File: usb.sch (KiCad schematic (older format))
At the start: 13 parts

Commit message: gpio assignment done
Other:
- note added: "tantalum cap"
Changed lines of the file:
@@
 $Descr A4 11693 8268
 encoding utf-8
-Sheet 8 10
+Sheet 7 10
 Title ""
 Date ""
@@
 Text Label 7500 3250 0    60   ~ 0
 USB1_PWR
+Text Notes 6625 4475 0    60   ~ 0
+tantalum cap
 $EndSCHEMATC

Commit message: annotation, wip erc
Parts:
- gave numbers to parts that had none: 13
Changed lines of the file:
@@
 $EndDescr
 $Comp
-L AM335X_ZCZ IC?
+L AM335X_ZCZ IC2
 U 11 1 58AF2AA9
 P 2300 2650
-F 0 "IC?" V 2250 2950 60  0000 C CNN
+F 0 "IC2" V 2250 2950 60  0000 C CNN
 F 1 "AM335X_ZCZ" V 2250 2350 60  0000 C CNN
 F 2 "footprints:PBGA_N324" H 2300 2650 60  0001 C CNN
@@
 	3800 2150 6025 2150
 $Comp
-L TPD4S012 U?
+L TPD4S012 U6
 U 1 1 58ACA818
 P 4400 3950
-F 0 "U?" H 4475 3700 60  0000 C CNN
+F 0 "U6" H 4475 3700 60  0000 C CNN
 F 1 "TPD4S012" H 4650 3600 60  0000 C CNN
 F 2 "" H 4425 4025 60  0001 C CNN
@@
 	3800 2350 6025 2350
 $Comp
-L USB_DC #PWR?
+L USB_DC #PWR253
 U 1 1 58ACAA5E
 P 4900 3450
-F 0 "#PWR?" H 4900 3300 50  0001 C CNN
+F 0 "#PWR253" H 4900 3300 50  0001 C CNN
 F 1 "USB_DC" H 4900 3600 50  0000 C CNN
 F 2 "" H 4900 3450 50  0000 C CNN
@@
 $EndComp
 $Comp
-L C C?
+L C C125
 U 1 1 58ACAA92
 P 4900 3850
-F 0 "C?" H 4925 3950 50  0000 L CNN
+F 0 "C125" H 4925 3950 50  0000 L CNN
 F 1 "100nF/6.3V" H 4925 3750 50  0000 L CNN
 F 2 "" H 4938 3700 50  0000 C CNN
@@
 Connection ~ 4900 3500
 $Comp
-L GNDD #PWR?
+L GNDD #PWR250
 U 1 1 58ACAB63
 P 4400 4425
-F 0 "#PWR?" H 4400 4175 50  0001 C CNN
+F 0 "#PWR250" H 4400 4175 50  0001 C CNN
 F 1 "GNDD" H 4400 4275 50  0000 C CNN
 F 2 "" H 4400 4425 50  0000 C CNN
@@
 NoConn ~ 3800 2450
 $Comp
-L R R?
+L R R52
 U 1 1 58ACACC5
 P 4675 2250
-F 0 "R?" V 4625 2050 50  0000 C CNN
+F 0 "R52" V 4625 2050 50  0000 C CNN
 F 1 "0R" V 4675 2250 50  0000 C CNN
 F 2 "" V 4605 2250 50  0000 C CNN
@@
 $EndComp
 $Comp
-L USB_DC #PWR?
+L USB_DC #PWR251
 U 1 1 58ACAD7C
 P 4825 2250
-F 0 "#PWR?" H 4825 2100 50  0001 C CNN
+F 0 "#PWR251" H 4825 2100 50  0001 C CNN
 F 1 "USB_DC" V 4825 2500 50  0000 C CNN
 F 2 "" H 4825 2250 50  0000 C CNN
@@
 	4525 2250 3800 2250
 $Comp
-L TPD4S012 U?
+L TPD4S012 U7
 U 1 1 58ACB0F7
 P 5700 3950
-F 0 "U?" H 5775 3700 60  0000 C CNN
+F 0 "U7" H 5775 3700 60  0000 C CNN
 F 1 "TPD4S012" H 5950 3600 60  0000 C CNN
 F 2 "" H 5725 4025 60  0001 C CNN
@@
 $EndComp
 $Comp
-L C C?
+L C C126
 U 1 1 58ACB106
 P 6200 3850
-F 0 "C?" H 6225 3950 50  0000 L CNN
+F 0 "C126" H 6225 3950 50  0000 L CNN
 F 1 "100nF/6.3V" H 6225 3750 50  0000 L CNN
 F 2 "" H 6238 3700 50  0000 C CNN
@@
 	6200 3250 6200 3700
 $Comp
-L GNDD #PWR?
+L GNDD #PWR254
 U 1 1 58ACB114
 P 5700 4425
-F 0 "#PWR?" H 5700 4175 50  0001 C CNN
+F 0 "#PWR254" H 5700 4175 50  0001 C CNN
 F 1 "GNDD" H 5700 4275 50  0000 C CNN
 F 2 "" H 5700 4425 50  0000 C CNN
@@
 NoConn ~ 3800 3250
 $Comp
-L R R?
+L R R53
 U 1 1 58ACB512
 P 4675 3050
-F 0 "R?" V 4775 3050 50  0000 C CNN
+F 0 "R53" V 4775 3050 50  0000 C CNN
 F 1 "0R" V 4675 3050 50  0000 C CNN
 F 2 "" V 4605 3050 50  0000 C CNN
@@
 	4525 3050 3800 3050
 $Comp
-L GNDD #PWR?
+L GNDD #PWR252
 U 1 1 58ACB72B
 P 4825 3050
-F 0 "#PWR?" H 4825 2800 50  0001 C CNN
+F 0 "#PWR252" H 4825 2800 50  0001 C CNN
 F 1 "GNDD" V 4825 2850 50  0000 C CNN
 F 2 "" H 4825 3050 50  0000 C CNN
@@
 Connection ~ 5650 2850
 $Comp
-L TPS2065CDGN U?
+L TPS2065CDGN U8
 U 1 1 58ACBDB9
 P 7800 3925
-F 0 "U?" H 7625 4300 60  0000 C CNN
+F 0 "U8" H 7625 4300 60  0000 C CNN
 F 1 "TPS2065CDGN" H 7875 4200 60  0000 C CNN
 F 2 "" H 7550 3600 60  0001 C CNN
@@
 	3800 2950 6950 2950
 $Comp
-L L L?
+L L L9
 U 1 1 58ACBFF2
 P 7100 2950
-F 0 "L?" V 7050 2950 50  0000 C CNN
+F 0 "L9" V 7050 2950 50  0000 C CNN
 F 1 "0.1ohm 0805" V 7175 2950 50  0000 C CNN
 F 2 "" H 7100 2950 50  0000 C CNN
@@
 $EndComp
 $Comp
-L L L?
+L L L10
 U 1 1 58ACC1B4
 P 8875 2950
-F 0 "L?" V 8825 2950 50  0000 C CNN
+F 0 "L10" V 8825 2950 50  0000 C CNN
 F 1 "150ohm 1000mA" V 8950 2950 50  0000 C CNN
 F 2 "" H 8875 2950 50  0000 C CNN
@@
 	7350 3975 7350 4825
 $Comp
-L R R?
+L R R54
 U 1 1 58ACC71E
 P 7350 4975
-F 0 "R?" V 7430 4975 50  0000 C CNN
+F 0 "R54" V 7430 4975 50  0000 C CNN
 F 1 "10k" V 7350 4975 50  0000 C CNN
 F 2 "" V 7280 4975 50  0000 C CNN
@@
 Connection ~ 7350 4775
 $Comp
-L GNDD #PWR?
+L GNDD #PWR257
 U 1 1 58ACC7E4
 P 7350 5125
-F 0 "#PWR?" H 7350 4875 50  0001 C CNN
+F 0 "#PWR257" H 7350 4875 50  0001 C CNN
 F 1 "GNDD" H 7350 4975 50  0000 C CNN
 F 2 "" H 7350 5125 50  0000 C CNN
@@
 $EndComp
 $Comp
-L CP C?
+L CP C127
 U 1 1 58ACC8FE
 P 6850 4025
-F 0 "C?" H 6875 4125 50  0000 L CNN
+F 0 "C127" H 6875 4125 50  0000 L CNN
 F 1 "220uF/6.3V" H 6875 3925 50  0000 L CNN
 F 2 "Capacitors_Tantalum_SMD:CP_Tantalum_Case-A_EIA-3216-18_Reflow" H 6888 3875 50  0001 C CNN
@@
 Connection ~ 7300 3775
 $Comp
-L GNDD #PWR?
+L GNDD #PWR256
 U 1 1 58ACCD7F
 P 6850 4175
-F 0 "#PWR?" H 6850 3925 50  0001 C CNN
+F 0 "#PWR256" H 6850 3925 50  0001 C CNN
 F 1 "GNDD" H 6850 4025 50  0000 C CNN
 F 2 "" H 6850 4175 50  0000 C CNN
@@
 $EndComp
 $Comp
-L SYS_5V #PWR?
+L SYS_5V #PWR255
 U 1 1 58ACCF48
 P 6850 3725
-F 0 "#PWR?" H 6850 3575 50  0001 C CNN
+F 0 "#PWR255" H 6850 3575 50  0001 C CNN
 F 1 "SYS_5V" H 6850 3875 50  0000 C CNN
 F 2 "" H 6850 3725 50  0000 C CNN
@@
 Connection ~ 8350 3775
 $Comp
-L GNDD #PWR?
+L GNDD #PWR258
 U 1 1 58ACD3E3
 P 7800 4575
-F 0 "#PWR?" H 7800 4325 50  0001 C CNN
+F 0 "#PWR258" H 7800 4325 50  0001 C CNN
 F 1 "GNDD" H 7800 4425 50  0000 C CNN
 F 2 "" H 7800 4575 50  0000 C CNN
@@
 Connection ~ 7800 4525
 $Comp
-L R R?
+L R R55
 U 1 1 58ACD6CF
 P 8600 3875
-F 0 "R?" V 8680 3875 50  0000 C CNN
+F 0 "R55" V 8680 3875 50  0000 C CNN
 F 1 "10k" V 8600 3875 50  0000 C CNN
 F 2 "" V 8530 3875 50  0000 C CNN
@@
 $EndComp
 $Comp
-L VDD_3V3A #PWR?
+L VDD_3V3A #PWR259
 U 1 1 58ACD7EC
 P 8600 3725
-F 0 "#PWR?" H 8600 3575 50  0001 C CNN
+F 0 "#PWR259" H 8600 3575 50  0001 C CNN
 F 1 "VDD_3V3A" H 8600 3875 50  0000 C CNN
 F 2 "" H 8600 3725 50  0000 C CNN

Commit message: erc passed, sch first version
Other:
- moved on the sheet: L10
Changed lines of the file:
@@
 	3800 2350 6025 2350
 $Comp
-L USB_DC #PWR253
+L USB_DC #PWR0269
 U 1 1 58ACAA5E
 P 4900 3450
-F 0 "#PWR253" H 4900 3300 50  0001 C CNN
+F 0 "#PWR0269" H 4900 3300 50  0001 C CNN
 F 1 "USB_DC" H 4900 3600 50  0000 C CNN
 F 2 "" H 4900 3450 50  0000 C CNN
@@
 Connection ~ 4900 3500
 $Comp
-L GNDD #PWR250
+L GNDD #PWR0270
 U 1 1 58ACAB63
 P 4400 4425
-F 0 "#PWR250" H 4400 4175 50  0001 C CNN
+F 0 "#PWR0270" H 4400 4175 50  0001 C CNN
 F 1 "GNDD" H 4400 4275 50  0000 C CNN
 F 2 "" H 4400 4425 50  0000 C CNN
@@
 $EndComp
 $Comp
-L USB_DC #PWR251
+L USB_DC #PWR0271
 U 1 1 58ACAD7C
 P 4825 2250
-F 0 "#PWR251" H 4825 2100 50  0001 C CNN
+F 0 "#PWR0271" H 4825 2100 50  0001 C CNN
 F 1 "USB_DC" V 4825 2500 50  0000 C CNN
 F 2 "" H 4825 2250 50  0000 C CNN
@@
 	6200 3250 6200 3700
 $Comp
-L GNDD #PWR254
+L GNDD #PWR0272
 U 1 1 58ACB114
 P 5700 4425
-F 0 "#PWR254" H 5700 4175 50  0001 C CNN
+F 0 "#PWR0272" H 5700 4175 50  0001 C CNN
 F 1 "GNDD" H 5700 4275 50  0000 C CNN
 F 2 "" H 5700 4425 50  0000 C CNN
@@
 	4525 3050 3800 3050
 $Comp
-L GNDD #PWR252
+L GNDD #PWR0273
 U 1 1 58ACB72B
 P 4825 3050
-F 0 "#PWR252" H 4825 2800 50  0001 C CNN
+F 0 "#PWR0273" H 4825 2800 50  0001 C CNN
 F 1 "GNDD" V 4825 2850 50  0000 C CNN
 F 2 "" H 4825 3050 50  0000 C CNN
@@
 L L L10
 U 1 1 58ACC1B4
-P 8875 2950
-F 0 "L10" V 8825 2950 50  0000 C CNN
-F 1 "150ohm 1000mA" V 8950 2950 50  0000 C CNN
-F 2 "" H 8875 2950 50  0000 C CNN
-F 3 "" H 8875 2950 50  0000 C CNN
-	1    8875 2950
+P 8800 2950
+F 0 "L10" V 8750 2950 50  0000 C CNN
+F 1 "150ohm 1000mA" V 8875 2950 50  0000 C CNN
+F 2 "" H 8800 2950 50  0000 C CNN
+F 3 "" H 8800 2950 50  0000 C CNN
+	1    8800 2950
 	0    1    1    0
 $EndComp
@@
 USB1_VBUS
 Wire Wire Line
-	9300 2950 9025 2950
-Wire Wire Line
-	7250 2950 8725 2950
+	8950 2950 9300 2950
+Wire Wire Line
+	7250 2950 8650 2950
 Wire Wire Line
 	3800 3150 3925 3150
@@
 Connection ~ 7350 4775
 $Comp
-L GNDD #PWR257
+L GNDD #PWR0274
 U 1 1 58ACC7E4
 P 7350 5125
-F 0 "#PWR257" H 7350 4875 50  0001 C CNN
+F 0 "#PWR0274" H 7350 4875 50  0001 C CNN
 F 1 "GNDD" H 7350 4975 50  0000 C CNN
 F 2 "" H 7350 5125 50  0000 C CNN
@@
 Connection ~ 7300 3775
 $Comp
-L GNDD #PWR256
+L GNDD #PWR0275
 U 1 1 58ACCD7F
 P 6850 4175
-F 0 "#PWR256" H 6850 3925 50  0001 C CNN
+F 0 "#PWR0275" H 6850 3925 50  0001 C CNN
 F 1 "GNDD" H 6850 4025 50  0000 C CNN
 F 2 "" H 6850 4175 50  0000 C CNN
@@
 $EndComp
 $Comp
-L SYS_5V #PWR255
+L SYS_5V #PWR0276
 U 1 1 58ACCF48
 P 6850 3725
-F 0 "#PWR255" H 6850 3575 50  0001 C CNN
+F 0 "#PWR0276" H 6850 3575 50  0001 C CNN
 F 1 "SYS_5V" H 6850 3875 50  0000 C CNN
 F 2 "" H 6850 3725 50  0000 C CNN
@@
 Connection ~ 8350 3775
 $Comp
-L GNDD #PWR258
+L GNDD #PWR0277
 U 1 1 58ACD3E3
 P 7800 4575
-F 0 "#PWR258" H 7800 4325 50  0001 C CNN
+F 0 "#PWR0277" H 7800 4325 50  0001 C CNN
 F 1 "GNDD" H 7800 4425 50  0000 C CNN
 F 2 "" H 7800 4575 50  0000 C CNN
@@
 $EndComp
 $Comp
-L VDD_3V3A #PWR259
+L VDD_3V3A #PWR0278
 U 1 1 58ACD7EC
 P 8600 3725
-F 0 "#PWR259" H 8600 3575 50  0001 C CNN
+F 0 "#PWR0278" H 8600 3575 50  0001 C CNN
 F 1 "VDD_3V3A" H 8600 3875 50  0000 C CNN
 F 2 "" H 8600 3725 50  0000 C CNN
@@
 Text Notes 6625 4475 0    60   ~ 0
 tantalum cap
+$Comp
+L PWR_FLAG #FLG0279
+U 1 1 58C56F63
+P 9250 3025
+F 0 "#FLG0279" H 9250 3100 50  0001 C CNN
+F 1 "PWR_FLAG" H 9250 3175 50  0000 C CNN
+F 2 "" H 9250 3025 50  0001 C CNN
+F 3 "" H 9250 3025 50  0001 C CNN
+	1    9250 3025
+	-1   0    0    1
+$EndComp
+Wire Wire Line
+	9250 3025 9250 2950
+Connection ~ 9250 2950
 $EndSCHEMATC

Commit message: wip sys and power
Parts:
- removed IC2: AM335X_ZCZ, footprints:PBGA_N324, symbol AM335X_ZCZ
- added C?: 100nF/6.3V, symbol C
- added IC?: OSD335x, GHI-SoMs-Processors_OSD3358, symbol OSD335x
- added IC?: SN74LVC2G241DCUR, symbol LOGIC-2G125_Dual_3ST_NonInv_Buffer
- added R?: 100k, symbol R
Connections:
- net GNDD: now also C?.2, IC?.1 (n1OE), IC?.4 (GND), R?.2
- net USB0_DM: now also IC?.N18 (USB0_DM)
- net USB0_DP: now also IC?.N17 (USB0_DP)
- net USB0_ID: now also IC?.P16 (USB0_ID)
- net USB1_DM: now also IC?.R18 (USB1_DM)
- net USB1_DP: now also IC?.R17 (USB1_DP)
- net USB1_DRVVBUS: now also IC?.F15 (USB1_DRVVBUS)
- net at R52.2: now also IC?.P15 (USB0_VBUS)
- net at R53.2: now also IC?.P17 (USB1_ID)
- net at L9.2: now also IC?.T18 (USB1_VBUS)
- new net UART0_RXD: IC?.2 (1A), R?.1
- new net UART0_RXD.CPU: IC?.6 (1Y), IC?.E15 (UART0_RXD)
- new net UART0_TXD: IC?.3 (2Y)
- new net UART0_TXD.CPU: IC?.5 (2A), IC?.E16 (UART0_TXD)
- new net VDD_3V3B: C?.1, IC?.7 (2OE), IC?.8 (VCC)
- no-connect marks 4 -> 6
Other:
- moved on the sheet: C125, C126, C127, L10, L9, R52, R53, R54, R55, U6, U7, U8

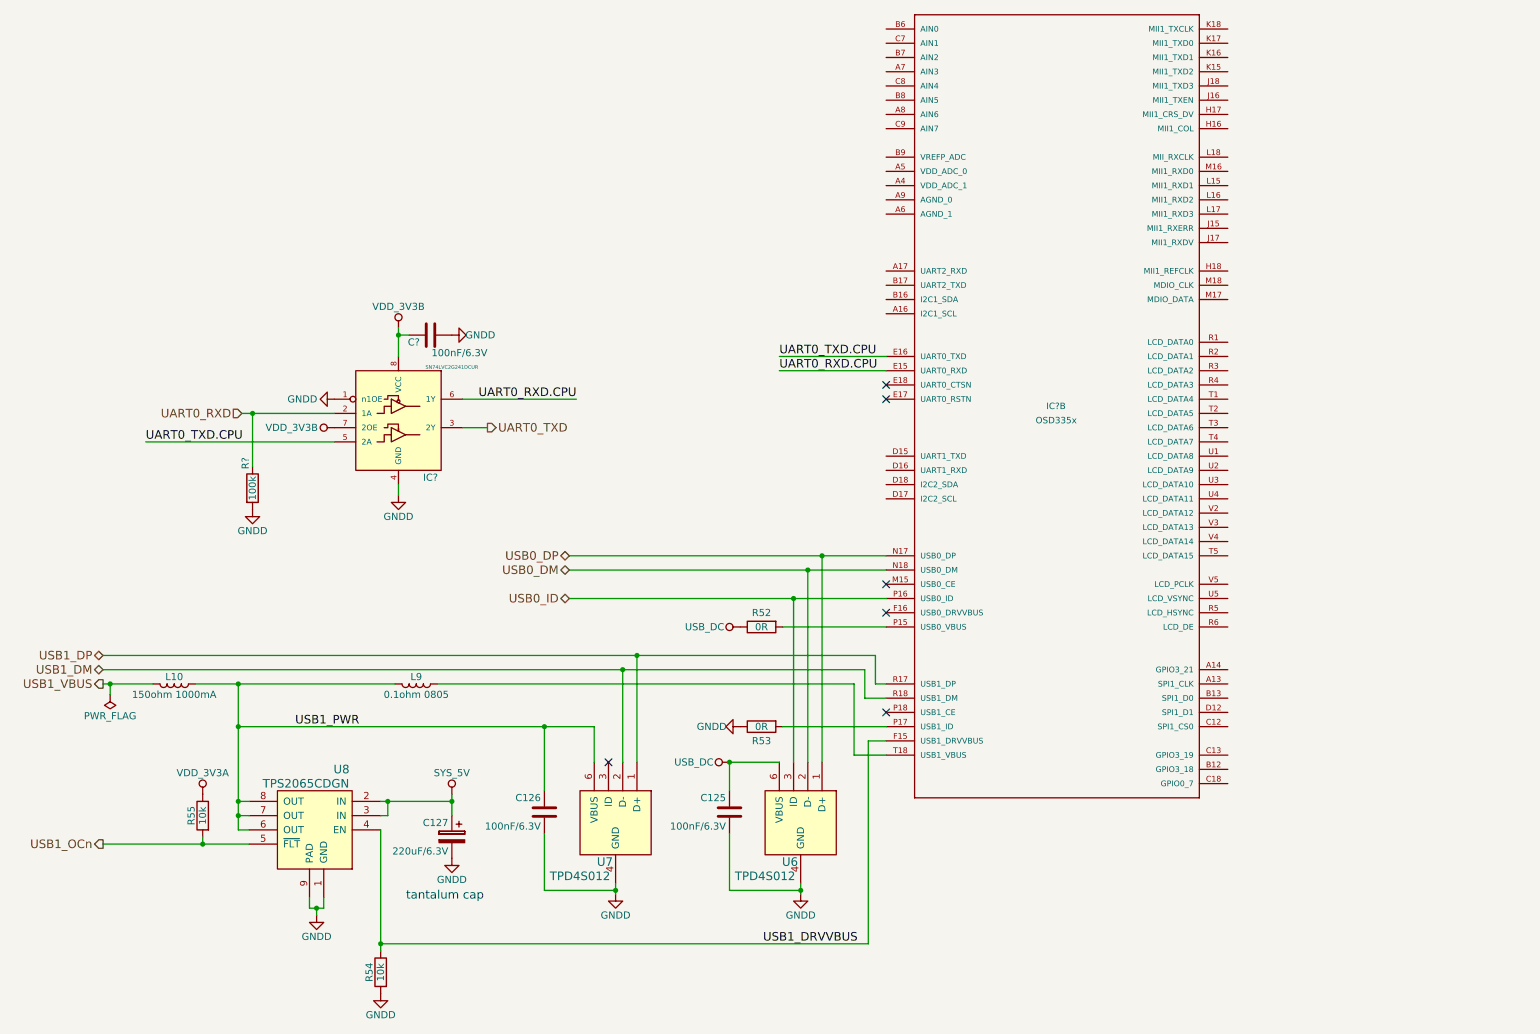
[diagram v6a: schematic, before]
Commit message: only io connectors remaining
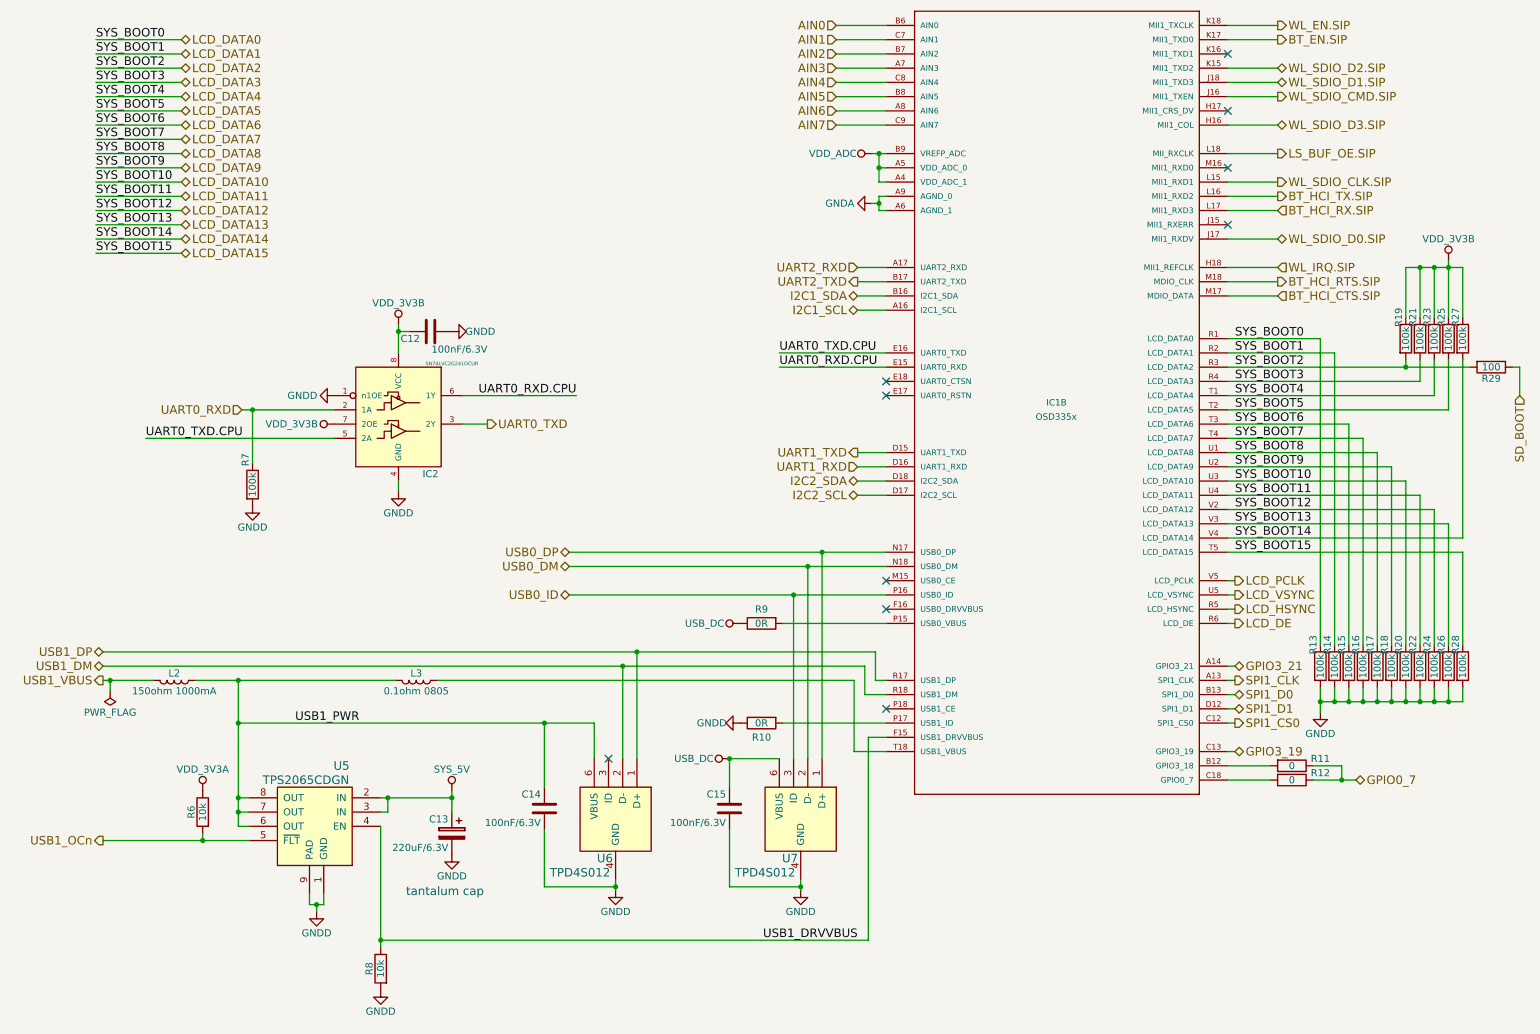
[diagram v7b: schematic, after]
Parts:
- added R11, R12: 0, symbol R
- added R13, R14, R15, R16, R17, R18, R19, R20, R21, R22, R23, R24, R25, R26, R27, R28: 100k, symbol R
- added R29: 100, symbol R
- gave numbers to parts that had none: 4
- renumbered C127 to C13, C126 to C14, C125 to C15, L10 to L2, L9 to L3, R53 to R10, R55 to R6, R54 to R8, R52 to R9, U8 to U5, U7 to U6, U6 to U7
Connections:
- net GNDD: now also R13.2, R14.2, R15.2, R16.2, R17.2, R18.2, R20.2, R22.2, R24.2, R26.2, R28.2
- net VDD_3V3B: now also R19.1, R21.1, R23.1, R25.1, R27.1
- net SPI1_CLK: now reaches IC1.A13 (SPI1_CLK)
- net GPIO3_21: now reaches IC1.A14 (GPIO3_21)
- net I2C1_SCL: now reaches IC1.A16 (I2C1_SCL)
- net UART2_RXD: now reaches IC1.A17 (UART2_RXD)
- net VDD_ADC: now reaches IC1.A4 (VDD_ADC_1)
- net VDD_ADC: now also IC1.A5 (VDD_ADC_0), IC1.B9 (VREFP_ADC)
- net GNDA: now reaches IC1.A6 (AGND_1)
- net GNDA: now also IC1.A9 (AGND_0)
- net AIN3: now reaches IC1.A7 (AIN3)
- net AIN6: now reaches IC1.A8 (AIN6)
- net at IC1.B12 (GPIO3_18): now also R11.2
- net SPI1_D0: now reaches IC1.B13 (SPI1_D0)
- net I2C1_SDA: now reaches IC1.B16 (I2C1_SDA)
- net UART2_TXD: now reaches IC1.B17 (UART2_TXD)
- net AIN0: now reaches IC1.B6 (AIN0)
- net AIN2: now reaches IC1.B7 (AIN2)
- net AIN5: now reaches IC1.B8 (AIN5)
- net SPI1_CS0: now reaches IC1.C12 (SPI1_CS0)
- net GPIO3_19: now reaches IC1.C13 (GPIO3_19)
- net at IC1.C18 (GPIO0_7): now also R12.2
- net AIN1: now reaches IC1.C7 (AIN1)
- net AIN4: now reaches IC1.C8 (AIN4)
- net AIN7: now reaches IC1.C9 (AIN7)
- net SPI1_D1: now reaches IC1.D12 (SPI1_D1)
- net UART1_TXD: now reaches IC1.D15 (UART1_TXD)
- net UART1_RXD: now reaches IC1.D16 (UART1_RXD)
- net I2C2_SCL: now reaches IC1.D17 (I2C2_SCL)
- net I2C2_SDA: now reaches IC1.D18 (I2C2_SDA)
- net WL_SDIO_D3.SIP: now reaches IC1.H16 (MII1_COL)
- net WL_IRQ.SIP: now reaches IC1.H18 (MII1_REFCLK)
- net WL_SDIO_CMD.SIP: now reaches IC1.J16 (MII1_TXEN)
- net WL_SDIO_D0.SIP: now reaches IC1.J17 (MII1_RXDV)
- net WL_SDIO_D1.SIP: now reaches IC1.J18 (MII1_TXD3)
- net WL_SDIO_D2.SIP: now reaches IC1.K15 (MII1_TXD2)
- net BT_EN.SIP: now reaches IC1.K17 (MII1_TXD0)
- net WL_EN.SIP: now reaches IC1.K18 (MII1_TXCLK)
- net WL_SDIO_CLK.SIP: now reaches IC1.L15 (MII1_RXD1)
- net BT_HCI_TX.SIP: now reaches IC1.L16 (MII1_RXD2)
- net BT_HCI_RX.SIP: now reaches IC1.L17 (MII1_RXD3)
- net LS_BUF_OE.SIP: now reaches IC1.L18 (MII_RXCLK)
- net BT_HCI_CTS.SIP: now reaches IC1.M17 (MDIO_DATA)
- net BT_HCI_RTS.SIP: now reaches IC1.M18 (MDIO_CLK)
- net LCD_DATA0: now reaches IC1.R1 (LCD_DATA0)
- net LCD_DATA0: now also R13.1
- net LCD_DATA1: now reaches IC1.R2 (LCD_DATA1)
- net LCD_DATA1: now also R14.1
- net LCD_DATA2: now reaches IC1.R3 (LCD_DATA2)
- net LCD_DATA2: now also R19.2, R29.2
- net LCD_DATA3: now reaches IC1.R4 (LCD_DATA3)
- net LCD_DATA3: now also R21.2
- net LCD_HSYNC: now reaches IC1.R5 (LCD_HSYNC)
- net LCD_DE: now reaches IC1.R6 (LCD_DE)
- net LCD_DATA4: now reaches IC1.T1 (LCD_DATA4)
- net LCD_DATA4: now also R23.2
- net LCD_DATA5: now reaches IC1.T2 (LCD_DATA5)
- net LCD_DATA5: now also R25.2
- net LCD_DATA6: now reaches IC1.T3 (LCD_DATA6)
- net LCD_DATA6: now also R15.1
- net LCD_DATA7: now reaches IC1.T4 (LCD_DATA7)
- net LCD_DATA7: now also R16.1
- net LCD_DATA15: now reaches IC1.T5 (LCD_DATA15)
- net LCD_DATA15: now also R28.1
- net LCD_DATA8: now reaches IC1.U1 (LCD_DATA8)
- net LCD_DATA8: now also R17.1
- net LCD_DATA9: now reaches IC1.U2 (LCD_DATA9)
- net LCD_DATA9: now also R18.1
- net LCD_DATA10: now reaches IC1.U3 (LCD_DATA10)
- net LCD_DATA10: now also R20.1
- net LCD_DATA11: now reaches IC1.U4 (LCD_DATA11)
- net LCD_DATA11: now also R22.1
- net LCD_VSYNC: now reaches IC1.U5 (LCD_VSYNC)
- net LCD_DATA12: now reaches IC1.V2 (LCD_DATA12)
- net LCD_DATA12: now also R24.1
- net LCD_DATA13: now reaches IC1.V3 (LCD_DATA13)
- net LCD_DATA13: now also R26.1
- net LCD_DATA14: now reaches IC1.V4 (LCD_DATA14)
- net LCD_DATA14: now also R27.2
- net LCD_PCLK: now reaches IC1.V5 (LCD_PCLK)
- new net GPIO0_7: R11.1, R12.1
- new net SD_BOOT: R29.1
- no-connect marks 6 -> 10
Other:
- moved on the sheet: C12, C13, C14, C15, IC1B, IC2, L2, L3, R10, R6, R7, R8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
